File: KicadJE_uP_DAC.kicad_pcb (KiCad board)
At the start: 2 copper layers, 100 x 100 mm, 216 parts, among them J201 CV1, J202 CV2, J203 OUT1, J204 OUT2, J205 IN1, J206 IN2, J301 AVR-ISP-6, J302 UART, J401 CV1, J402 CV2, J403 OUT1, J404 OUT2, J405 OUT3, J406 OUT4, J407 IN1, J408 IN2, J409 I2C, J501 BOOT, J502 UART, J503 USB_B_Micro, P201 Doepfer_Power_16pin, P401 Doepfer_Power_16pin, SW201 SW_SPDT, SW401 SW_SPDT, U201 TL072, U202 MCP4822, U301 ATmega32A-AU, U401 TL072, U402 TL072, U405 MCP4822, U501 AMS1117-3.3, U502 STM32F103C8Tx, Y301 16MHz, Y501 8 MHz

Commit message: Connectors arount STM32
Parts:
- JP406: value PWM_1 -> PWM1
- JP407: value PWM_2 -> PWM2
- moved JP405 103.2 mm to (87.0, 101.5), turned to 0 degrees
- moved R511 96.9 mm to (64.0, 65.0)
- moved R512 94.0 mm to (64.0, 67.0)
- moved R510 93.7 mm to (77.5, 90.0)
- moved R507 91.3 mm to (64.0, 58.8), turned to 0 degrees
- moved R509 88.4 mm to (71.5, 87.5), turned to 0 degrees
- moved J409 75.7 mm to (83.0, 85.9), turned to 180 degrees
- moved J502 52.5 mm to (62.8, 86.2), turned to 0 degrees
- moved J503 47.4 mm to (54.5, 66.5), turned to 90 degrees
- moved R505 42.0 mm to (58.0, 107.5), turned to 90 degrees
- moved JP406 32.0 mm to (74.6, 109.4)
- moved JP407 31.1 mm to (77.5, 109.4)
- moved JP404 21.8 mm to (84.0, 101.5), turned to 0 degrees
- moved JP403 20.0 mm to (81.0, 101.5), turned to 0 degrees
- moved C504 0.62 mm to (73.0, 89.9)
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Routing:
- net /KicadJE_STM32F0/STM32F103C8/STM32_SWCLK_PA14: track 0.00 -> 23.7 mm
- net /KicadJE_STM32F0/STM32F103C8/STM32_SWDIO_PA13: track 0.00 -> 14.5 mm
- net /KicadJE_STM32F0/STM32F103C8/STM32_Boot0: track 0.00 -> 13.9 mm
- net /KicadJE_STM32F0/STM32F103C8/STM32_boot1_PB2: track 0.00 -> 10.8 mm
- net STM_DACB: track 0.00 -> 9.69 mm
- net STM_DACA: track 0.00 -> 8.99 mm
- net Net-(J501-Pad3): track 0.00 -> 5.48 mm
- net GND: track 62.2 -> 66.7 mm
- net boot_0: track 0.00 -> 2.85 mm
- added copper zone on B.Cu, net +3V3

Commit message: PCB
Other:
- board text added: "DDS 1"
- board text added: "DDS 2"
- board text added: "EU-6 Delay Line"
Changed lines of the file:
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@@
   (general
     (thickness 1.6)
-    (drawings 38)
+    (drawings 39)
     (tracks 1028)
     (zones 0)
@@
     )
   )
-  (gr_text "VCO3 " (at 113 165 90) (layer F.SilkS)
+  (gr_text "DDS 2" (at 84.25 161.25 90) (layer F.SilkS)
+    (effects (font (size 4 4) (thickness 0.25)))
+  )
+  (gr_text "DDS 1" (at 117.25 161 90) (layer F.SilkS)
     (effects (font (size 4 4) (thickness 0.25)))
   )
@@
     (effects (font (size 1.8 1.8) (thickness 0.25)) (justify mirror))
   )
-  (gr_text "EU-4 Reverb" (at 43 129.25 270) (layer F.SilkS)
+  (gr_text "EU-6 Delay Line" (at 32.25 151.5 270) (layer F.SilkS)
     (effects (font (size 2 2) (thickness 0.3)))
   )

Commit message: serial to DAC - STM32
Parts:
- C501, C507, Y501: moved to F.Cu
- moved R408 153.1 mm to (82.3, 154.5)
- moved C406 149.4 mm to (81.6, 159.6)
- moved R412 134.8 mm to (75.1, 154.8)
- moved R405 122.2 mm to (67.2, 159.1)
- moved R406 120.0 mm to (73.4, 160.7)
- moved D419 50.3 mm to (43.1, 39.0)
- moved D404 49.8 mm to (48.2, 39.0)
- moved C507 49.3 mm to (68.8, 100.0), turned to 0 degrees
- moved C501 48.5 mm to (72.5, 100.0)
- moved Y501 47.7 mm to (73.2, 103.8)
- moved C408 42.2 mm to (45.7, 104.0)
- moved D413 41.0 mm to (54.7, 36.1)
- moved D422 41.0 mm to (54.7, 39.4)
- moved D409 38.9 mm to (37.8, 39.1)
- moved C414 31.4 mm to (45.5, 100.1)
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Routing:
- net +3V3: track 37.9 -> 85.3 mm, vias 0 -> 2
- net /KicadJE_STM32F0/STM32F103C8/STM32_PB15: track 0.00 -> 24.9 mm, vias 0 -> 2
- net /KicadJE_STM32F0/STM32F103C8/STM32_PB13: track 0.00 -> 24.6 mm
- net /KicadJE_STM32F0/STM32F103C8/STM32_PB12: track 0.00 -> 21.8 mm
- net Net-(J407-PadTN): track 0.00 -> 20.2 mm, vias 0 -> 2
- net Net-(JP405-Pad1): track 0.00 -> 18.8 mm
- net Net-(J401-PadTN): track 0.00 -> 18.6 mm, vias 0 -> 2
- net Net-(JP404-Pad1): track 0.00 -> 17.8 mm
- net /KicadJE_STM32F0/STM32F103C8/STM32_SCL1_PWM_PB8: track 0.00 -> 15.7 mm, vias 0 -> 2
- net Net-(JP403-Pad1): track 0.00 -> 15.5 mm
- net Net-(J503-Pad1): track 0.00 -> 14.4 mm
- net /KicadJE_STM32F0/STM32F103C8/STM32_SDA1_PWM_PB9: track 0.00 -> 13.5 mm, vias 0 -> 2
- net GND: track 66.7 -> 79.5 mm, vias 7 -> 9
- net Net-(C501-Pad1): track 0.00 -> 10.2 mm
- net Net-(C507-Pad1): track 0.00 -> 8.90 mm
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
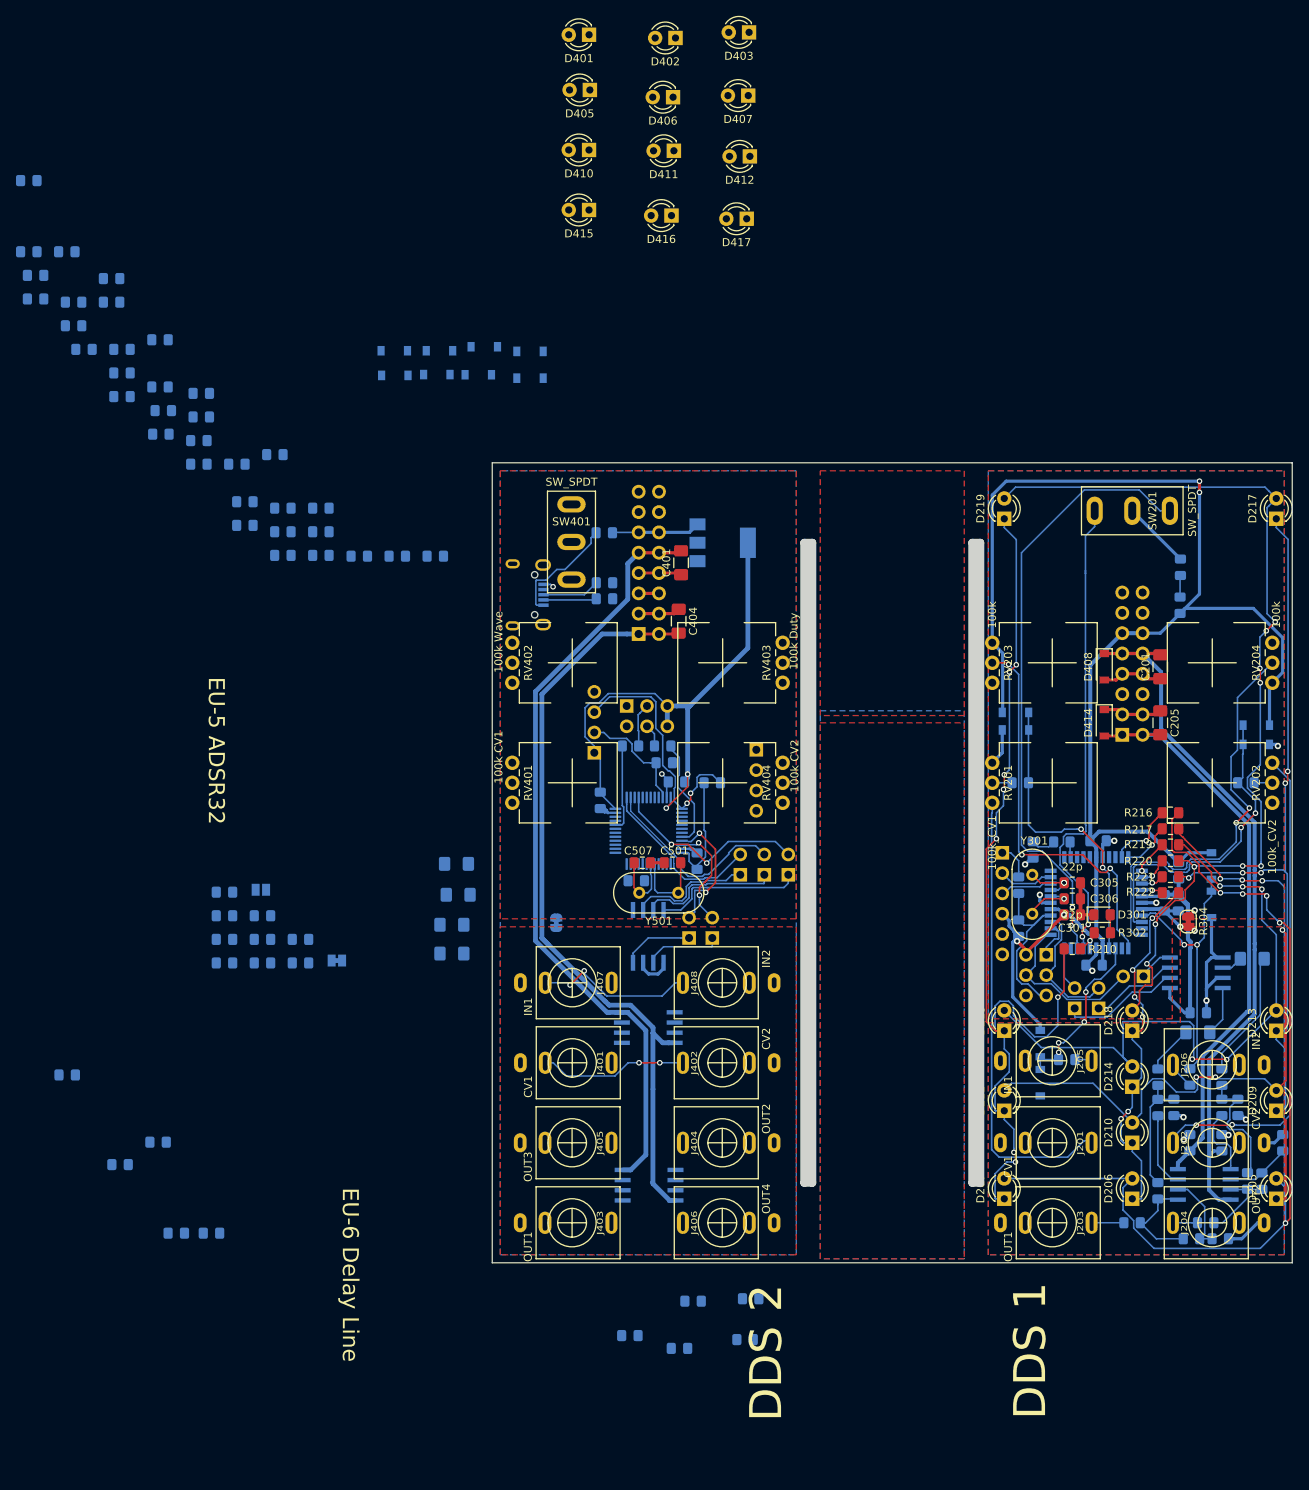
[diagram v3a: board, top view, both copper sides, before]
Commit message: Changed Op Amp A and B
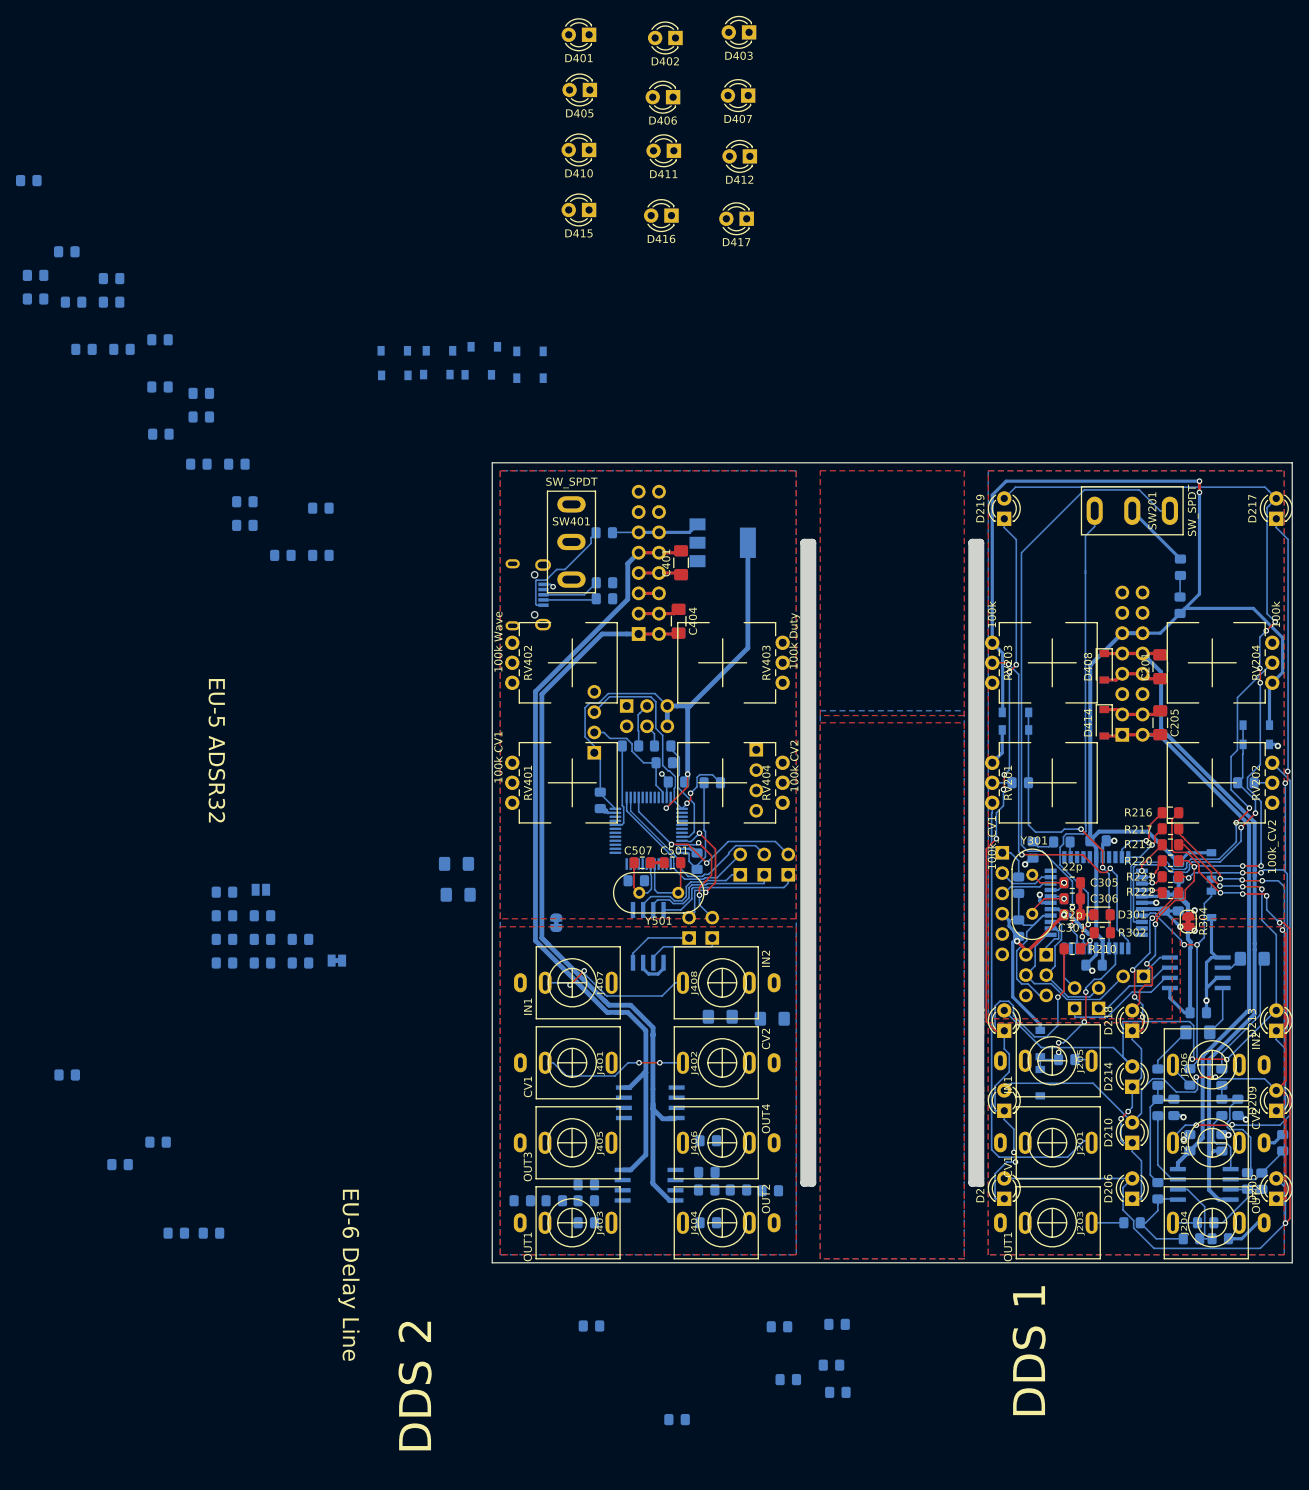
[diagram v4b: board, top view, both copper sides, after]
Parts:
- moved R413 151.6 mm to (62.4, 157.9)
- moved R419 129.1 mm to (61.8, 145.0), turned to 0 degrees
- moved R404 123.8 mm to (76.8, 138.7), turned to 0 degrees
- moved C411 114.1 mm to (57.8, 142.2)
- moved R420 113.9 mm to (77.0, 134.8)
- moved R403 113.5 mm to (73.1, 169.6)
- moved R422 106.7 mm to (61.8, 142.2), turned to 0 degrees
- moved R410 100.3 mm to (76.8, 140.9)
- moved C405 100.1 mm to (80.8, 140.9)
- moved R409 99.7 mm to (84.8, 141.0)
- moved R414 99.2 mm to (61.8, 140.2)
- moved R407 94.1 mm to (77.0, 145.0)
- moved R421 81.3 mm to (53.8, 142.2), turned to 0 degrees
- moved C407 41.7 mm to (85.0, 119.5)
- moved C413 34.5 mm to (78.5, 119.2)
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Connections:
- C407 pad 2: STM_DACA -> STM_DACB
- C408 pad 2: PWM_PA8 -> PWM_PA9
- C413 pad 2: STM_DACB -> STM_DACA
- C414 pad 2: PWM_PA9 -> PWM_PA8
- J403 pad T: (no net) -> STM32_OUT1
- J404 pad T: (no net) -> STM32_OUT2
- J405 pad T: (no net) -> STM32_OUT3
- J406 pad T: (no net) -> STM32_OUT4
- R407 pad 2: OUT1 -> STM32_OUT2
- R408 pad 2: (no net) -> STM32_OUT4
- R419 pad 2: OUT2 -> STM32_OUT1
- R420 pad 2: (no net) -> STM32_OUT3
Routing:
- net +12V: track 184.8 -> 188.3 mm
- net -12V: track 180.9 -> 181.8 mm

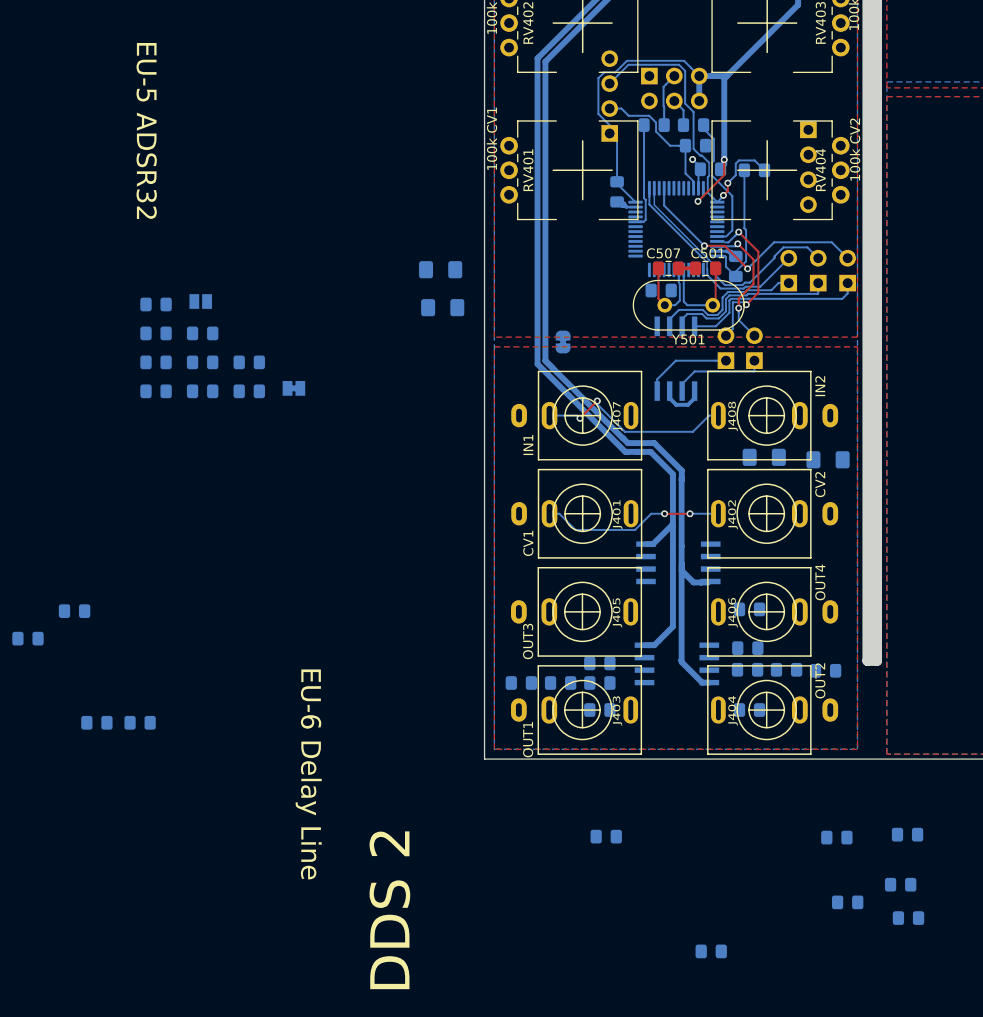
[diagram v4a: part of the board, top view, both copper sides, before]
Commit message: Output filter routing STM32
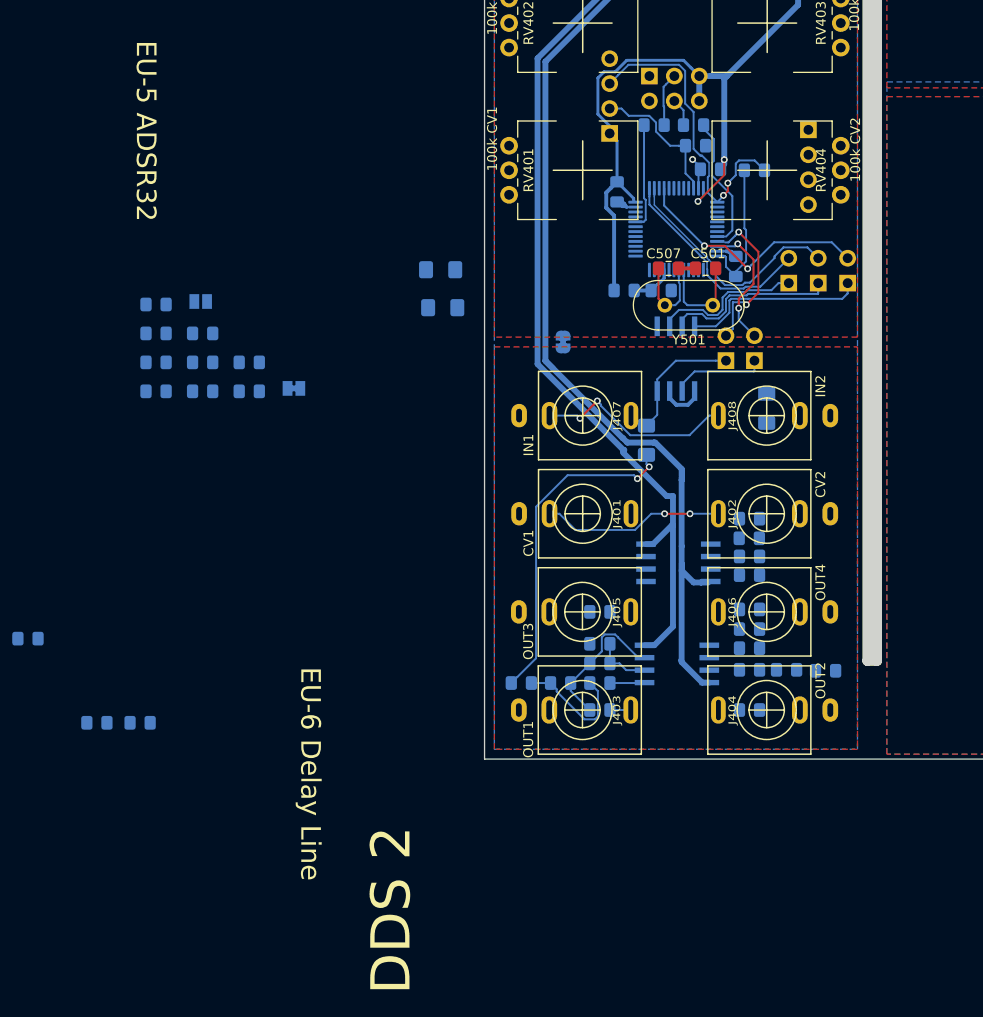
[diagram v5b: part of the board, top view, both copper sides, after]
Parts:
- moved R504 64.8 mm to (64.2, 102.2)
- moved R406 42.0 mm to (77.0, 127.5)
- moved C406 40.4 mm to (77.0, 125.5), turned to 0 degrees
- moved R405 36.6 mm to (77.0, 129.3)
- moved R403 33.1 mm to (77.0, 136.8)
- moved R412 28.2 mm to (77.0, 131.2)
- moved R408 28.0 mm to (77.0, 134.8)
- moved R413 19.7 mm to (61.8, 138.2), turned to 0 degrees
- moved R420 15.3 mm to (61.8, 135.0), turned to 0 degrees
- moved C413 12.1 mm to (66.5, 117.5), turned to 90 degrees
- moved C407 8.16 mm to (78.8, 114.2), turned to 90 degrees
- moved R410 0.20 mm to (77.0, 140.9)
- moved R404 0.17 mm to (77.0, 138.7)
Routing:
- net Net-(C413-Pad1): track 0.00 -> 33.8 mm, vias 0 -> 2
- net Net-(C411-Pad1): track 0.00 -> 15.0 mm
- net Net-(C411-Pad2): track 0.00 -> 12.3 mm
- net +3V3: track 85.3 -> 97.3 mm
- net Net-(R413-Pad2): track 0.00 -> 5.81 mm
- net +3.3VA: track 0.00 -> 4.41 mm
- net STM_DACA: track 8.99 -> 13.0 mm
- net Net-(R422-Pad2): track 0.00 -> 3.54 mm
- net STM32_OUT1: track 0.00 -> 2.12 mm
- net +12V: track 188.3 -> 186.6 mm
- net -12V: track 181.8 -> 182.5 mm
